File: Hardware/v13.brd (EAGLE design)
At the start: 50 x 50 mm, 90 parts, among them J1 22-27-2081-08, J2 22-27-2031-03

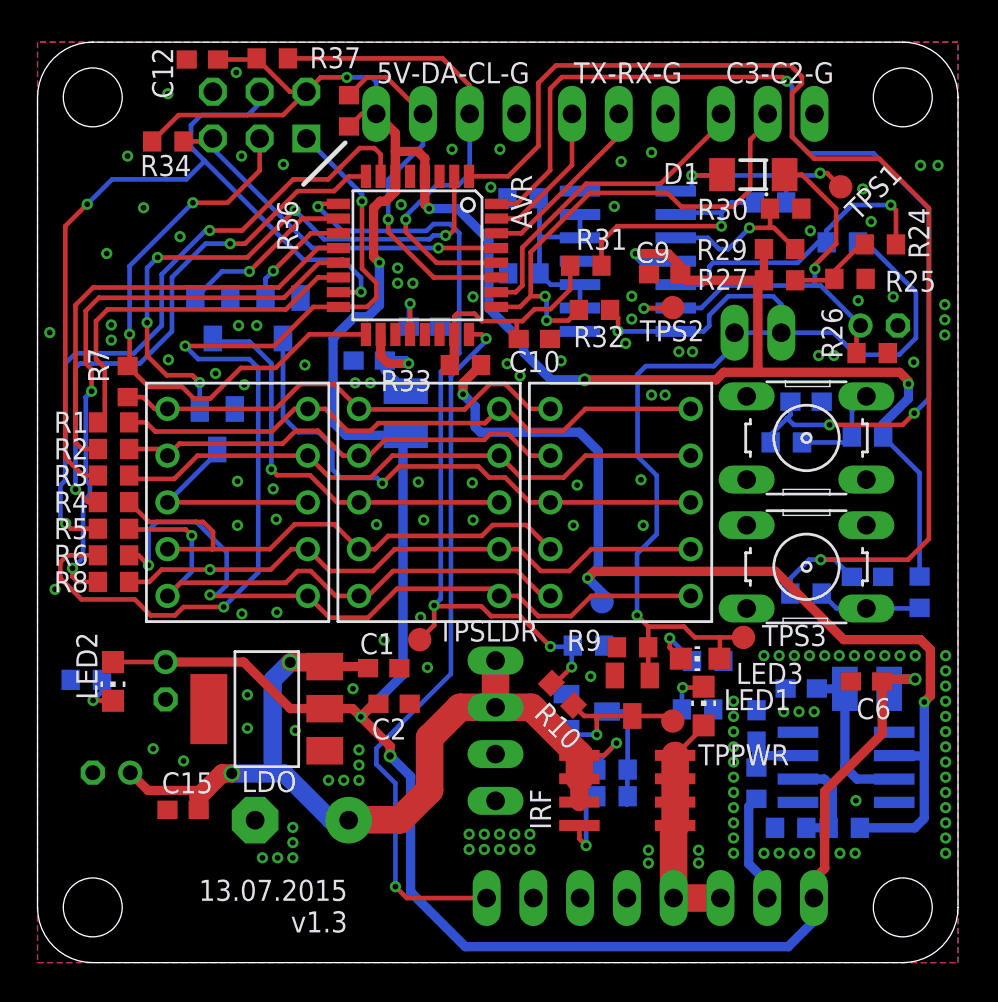
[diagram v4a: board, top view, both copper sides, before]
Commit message: changed the place of some resistors
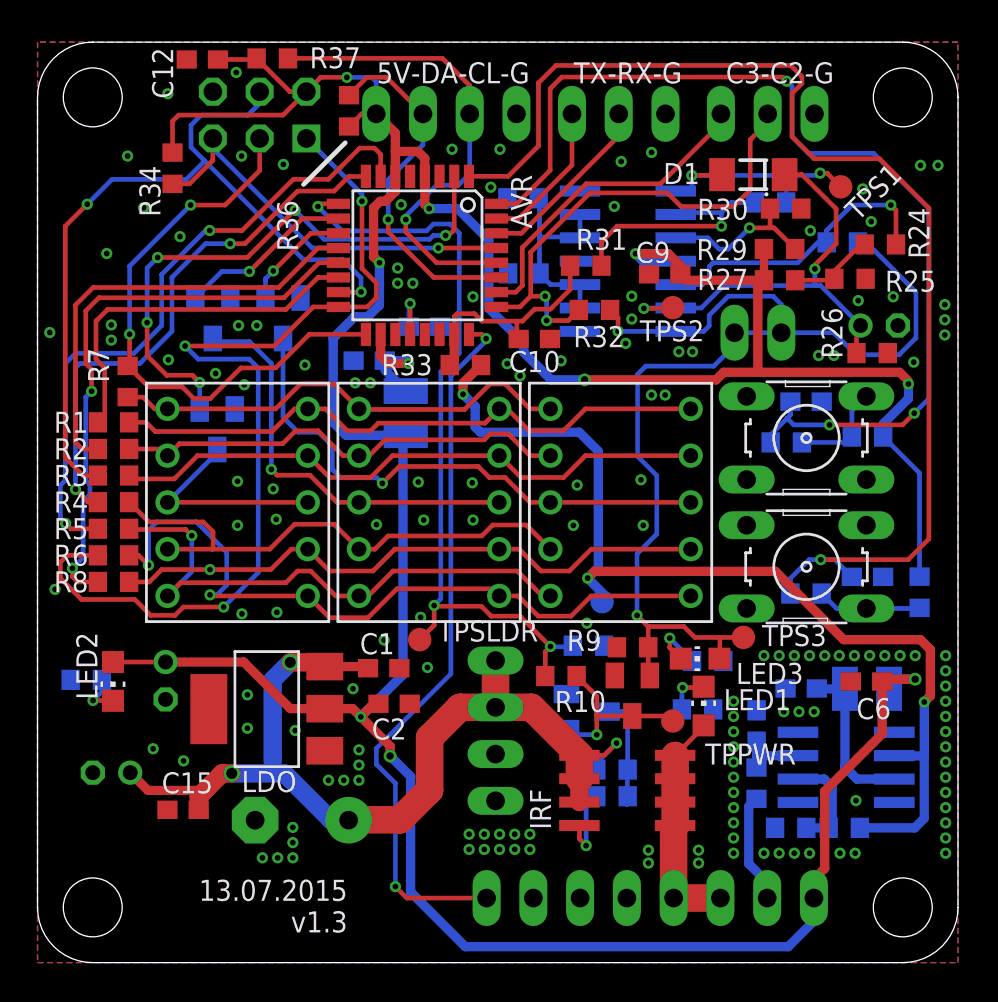
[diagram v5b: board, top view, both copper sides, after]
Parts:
- moved R34 1.48 mm to (7.33, 43.2), turned to 270 degrees
- moved R10 0.99 mm to (28.4, 15.6), turned to 180 degrees
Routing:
- net RST: track 19.9 -> 22.1 mm
- net N$16: track 8.96 -> 10.1 mm
- net LOETKOLBEN: track 43.9 -> 43.0 mm, vias 4 -> 3
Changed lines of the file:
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@@
 <layer number="20" name="Dimension" color="15" fill="1" visible="yes" active="yes"/>
 <layer number="21" name="tPlace" color="7" fill="1" visible="yes" active="yes"/>
-<layer number="22" name="bPlace" color="7" fill="1" visible="no" active="yes"/>
+<layer number="22" name="bPlace" color="7" fill="1" visible="yes" active="yes"/>
 <layer number="23" name="tOrigins" color="15" fill="1" visible="yes" active="yes"/>
-<layer number="24" name="bOrigins" color="15" fill="1" visible="no" active="yes"/>
+<layer number="24" name="bOrigins" color="15" fill="1" visible="yes" active="yes"/>
 <layer number="25" name="tNames" color="7" fill="1" visible="yes" active="yes"/>
 <layer number="26" name="bNames" color="7" fill="1" visible="no" active="yes"/>
@@
 <attribute name="VALUE" x="23.1775" y="31.75" size="1.27" layer="28" rot="MR270"/>
 </element>
-<element name="R34" library="rcl" package="R0603" value="10k" x="7.08025" y="44.605575" smashed="yes">
-<attribute name="NAME" x="5.578475" y="42.7228" size="1.143" layer="25" font="vector" ratio="15"/>
-<attribute name="VALUE" x="6.44525" y="42.700575" size="1.27" layer="27"/>
+<element name="R34" library="rcl" package="R0603" value="10k" x="7.33425" y="43.151425" smashed="yes" rot="R270">
+<attribute name="NAME" x="5.534025" y="43.291125" size="1.143" layer="25" font="vector" ratio="15" rot="R270"/>
+<attribute name="VALUE" x="5.42925" y="43.786425" size="1.27" layer="27" rot="R270"/>
 </element>
 <element name="DIS1" library="display-hp" package="HDSP-E" value="SC39-11SRWA" x="31.67" y="25" smashed="yes">
@@
 </element>
 <element name="R33" library="rcl" package="R0603" value="10k" x="23.241" y="32.458025" smashed="yes" rot="R180">
-<attribute name="NAME" x="18.63725" y="31.0388" size="1.143" layer="25" font="vector" ratio="15"/>
+<attribute name="NAME" x="18.678525" y="31.905575" size="1.143" layer="25" font="vector" ratio="15"/>
 <attribute name="VALUE" x="23.876" y="34.363025" size="1.27" layer="27" rot="R180"/>
 </element>
@@
 <attribute name="VALUE" x="30.56255" y="15.313025" size="1.27" layer="28" rot="MR0"/>
 </element>
-<element name="R10" library="rcl" package="R0603" value="10k" x="28.514675" y="14.576425" smashed="yes" rot="R135">
-<attribute name="NAME" x="29.670371875" y="12.275046875" size="1.143" layer="25" font="vector" ratio="15" rot="R135"/>
-<attribute name="VALUE" x="30.310725" y="15.47445" size="1.27" layer="27" rot="R135"/>
+<element name="R10" library="rcl" package="R0603" value="10k" x="28.432125" y="15.567025" smashed="yes" rot="R180">
+<attribute name="NAME" x="30.87664375" y="14.756903125" size="1.143" layer="25" font="vector" ratio="15" rot="R180"/>
+<attribute name="VALUE" x="29.067121875" y="17.472021875" size="1.27" layer="27" rot="R180"/>
 </element>
 <element name="R15" library="rcl" package="R0603" value="10k" x="31.2039" y="10.48385" smashed="yes" rot="MR0">
@@
 <element name="TPPWR" library="testpad" package="B1,27" value="TPB1,27" x="34.5059" y="13.12545" smashed="yes">
 <attribute name="TP_SIGNAL_NAME" value="" x="33.8709" y="11.22045" size="1" layer="37"/>
-<attribute name="NAME" x="35.893375" y="10.715625" size="1.143" layer="25" font="vector" ratio="15"/>
+<attribute name="NAME" x="36.26485" y="10.7569" size="1.143" layer="25" font="vector" ratio="15"/>
 <attribute name="VALUE" x="33.8709" y="12.36345" size="0.0254" layer="27"/>
 </element>
@@
 <wire x1="18.272125" y1="14.062075" x2="18.5175" y2="14.062075" width="0.508" layer="1"/>
 <wire x1="13.335" y1="46.0375" x2="7.662175" y2="46.0375" width="0.254" layer="1"/>
-<wire x1="7.662175" y1="46.0375" x2="6.23025" y2="44.605575" width="0.254" layer="1"/>
 <wire x1="9.8035" y1="49.056925" x2="11.84365" y2="49.056925" width="0.254" layer="1"/>
 <wire x1="11.84365" y1="49.056925" x2="11.903975" y2="49.11725" width="0.254" layer="1"/>
 <wire x1="14.605" y1="47.3075" x2="13.713725" y2="47.3075" width="0.254" layer="1"/>
 <wire x1="13.713725" y1="47.3075" x2="11.903975" y2="49.11725" width="0.254" layer="1"/>
+<wire x1="7.662175" y1="46.0375" x2="7.33425" y2="45.709575" width="0.254" layer="1"/>
+<wire x1="7.33425" y1="45.709575" x2="7.33425" y2="44.001425" width="0.254" layer="1"/>
 </signal>
 <signal name="GND">
@@
 <via x="44.45635" y="8.8011" extent="1-16" drill="0.31"/>
 <contactref element="C6" pad="1"/>
-<via x="30.0482" y="15.547975" extent="1-16" drill="0.31"/>
+<via x="29.841825" y="18.437225" extent="1-16" drill="0.31"/>
 <via x="37.8079" y="14.1986" extent="1-16" drill="0.31"/>
 <via x="39.4589" y="16.6751" extent="1-16" drill="0.31"/>
@@
 <contactref element="R10" pad="2"/>
 <wire x1="21.9075" y1="19.7612" x2="21.9075" y2="32.09925" width="0.254" layer="16"/>
-<via x="29.016325" y="16.055975" extent="1-16" drill="0.31"/>
-<wire x1="29.016325" y1="16.055975" x2="29.016325" y2="17.1568" width="0.254" layer="16"/>
 <wire x1="29.016325" y1="17.1568" x2="29.07755" y2="17.218025" width="0.254" layer="16"/>
 <wire x1="29.016325" y1="17.1568" x2="27.874225" y2="17.1568" width="0.254" layer="16"/>
@@
 <via x="21.54555" y="19.39925" extent="1-16" drill="0.31"/>
 <wire x1="21.54555" y1="19.39925" x2="21.9075" y2="19.7612" width="0.254" layer="16"/>
-<wire x1="29.016325" y1="16.055975" x2="28.137815625" y2="15.177465625" width="0.254" layer="1"/>
-<wire x1="28.137815625" y1="15.177465625" x2="27.91363125" y2="15.177465625" width="0.254" layer="1"/>
 <contactref element="TPSLDR" pad="TP"/>
 <wire x1="20.761325" y1="17.541875" x2="21.54555" y2="18.3261" width="0.254" layer="1"/>
@@
 <wire x1="22.907625" y1="39.624" x2="22.412325" y2="40.1193" width="0.254" layer="16"/>
 <wire x1="22.412325" y1="40.1193" x2="21.504275" y2="40.1193" width="0.254" layer="16"/>
+<wire x1="27.582125" y1="15.567025" x2="27.582125" y2="16.8919" width="0.254" layer="1"/>
+<wire x1="27.582125" y1="16.8919" x2="27.860625" y2="17.1704" width="0.254" layer="1"/>
 </signal>
 <signal name="MOSI">
@@
 <contactref element="R7" pad="2"/>
 <wire x1="17.8375" y1="34.1249" x2="17.820725" y2="34.108125" width="0.254" layer="1"/>
-<via x="8.43915" y="41.275" extent="1-16" drill="0.31"/>
+<via x="8.315325" y="41.151175" extent="1-16" drill="0.31"/>
 <wire x1="8.493125" y1="30.63875" x2="7.858125" y2="31.27375" width="0.254" layer="1"/>
 <wire x1="8.493125" y1="30.63875" x2="9.37895" y2="30.63875" width="0.254" layer="1"/>
@@
 <wire x1="12.938125" y1="32.305625" x2="14.7574" y2="34.1249" width="0.254" layer="1"/>
 <wire x1="5.000625" y1="34.13125" x2="5.000625" y2="37.836475" width="0.254" layer="16"/>
-<wire x1="5.000625" y1="37.836475" x2="8.43915" y2="41.275" width="0.254" layer="16"/>
-<wire x1="12.065" y1="43.02125" x2="10.31875" y2="41.275" width="0.254" layer="1"/>
-<wire x1="10.31875" y1="41.275" x2="8.43915" y2="41.275" width="0.254" layer="1"/>
+<wire x1="5.000625" y1="37.836475" x2="8.315325" y2="41.151175" width="0.254" layer="16"/>
+<wire x1="12.065" y1="43.02125" x2="10.194925" y2="41.151175" width="0.254" layer="1"/>
+<wire x1="10.194925" y1="41.151175" x2="8.315325" y2="41.151175" width="0.254" layer="1"/>
 <wire x1="12.065" y1="43.02125" x2="12.065" y2="44.7675" width="0.254" layer="1"/>
 <via x="5.000625" y="34.13125" extent="1-16" drill="0.31"/>
@@
 <wire x1="14.92255" y1="38.8175" x2="21.7742" y2="38.8175" width="0.254" layer="16"/>
 <via x="21.7742" y="38.8175" extent="1-16" drill="0.31"/>
-<wire x1="7.93025" y1="44.605575" x2="9.363075" y2="44.605575" width="0.254" layer="1"/>
-<wire x1="9.363075" y1="44.605575" x2="9.525" y2="44.7675" width="0.254" layer="1"/>
+<wire x1="7.33425" y1="42.301425" x2="8.24955" y2="42.301425" width="0.254" layer="1"/>
+<wire x1="8.24955" y1="42.301425" x2="9.525" y2="43.576875" width="0.254" layer="1"/>
+<wire x1="9.525" y1="43.576875" x2="9.525" y2="44.7675" width="0.254" layer="1"/>
 </signal>
 <signal name="12V">
@@
 <contactref element="PWR-Q2" pad="3"/>
 <wire x1="28.29945" y1="12.686625" x2="28.7323" y2="12.686625" width="0.254" layer="16"/>
-<wire x1="29.115715625" y1="13.97538125" x2="29.694046875" y2="13.39705" width="0.254" layer="1"/>
-<wire x1="29.694046875" y1="13.39705" x2="30.3784" y2="13.39705" width="0.254" layer="1"/>
 <wire x1="30.3784" y1="13.39705" x2="32.3088" y2="13.39705" width="0.254" layer="1"/>
 <wire x1="28.7323" y1="12.686625" x2="29.036425" y2="12.3825" width="0.254" layer="16"/>
@@
 <wire x1="34.5059" y1="13.12545" x2="34.2343" y2="13.39705" width="0.254" layer="1"/>
 <wire x1="34.2343" y1="13.39705" x2="32.3088" y2="13.39705" width="0.254" layer="1"/>
+<wire x1="30.3784" y1="13.39705" x2="30.3784" y2="14.47075" width="0.254" layer="1"/>
+<wire x1="30.3784" y1="14.47075" x2="29.282125" y2="15.567025" width="0.254" layer="1"/>
 </signal>
 <signal name="N$22">

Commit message: change some resistor values moved the leds to lower left corner
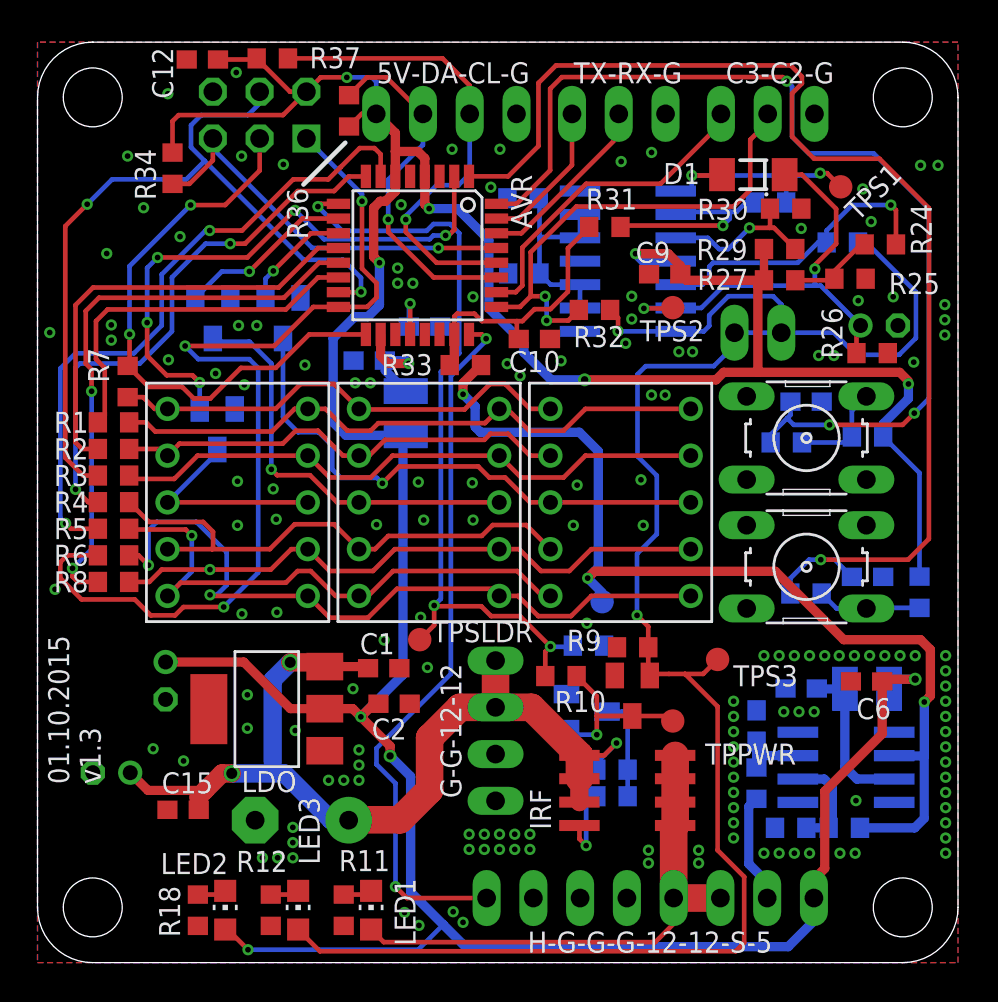
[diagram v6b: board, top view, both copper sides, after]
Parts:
- R31: value 20k -> 10k
- R36, R37: value 4k7 -> 10k
- moved R12 27.3 mm to (12.7, 2.85), flipped to the top, turned to 270 degrees
- moved LED3 25.8 mm to (14.2, 2.85), turned to 0 degrees
- moved R11 22.1 mm to (16.6, 2.85), flipped to the top, turned to 90 degrees
- moved LED1 21.2 mm to (18.1, 2.85)
- moved R18 13.9 mm to (8.71, 2.85), flipped to the top, turned to 90 degrees
- moved LED2 13.8 mm to (10.2, 2.85), turned to 0 degrees
- moved R31 2.34 mm to (30.8, 40.0)
- moved TPS3 1.84 mm to (36.9, 16.5)
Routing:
- net SAFETY: track 61.3 -> 99.6 mm
- net PWM_OUT: track 12.7 -> 28.9 mm
- net VCC: track 199.0 -> 209.0 mm, vias 9 -> 10
- net THERMO0: track 12.3 -> 14.8 mm
- net N$3: track 13.5 -> 11.1 mm
- net N$2: track 3.10 -> 1.57 mm, vias 1 -> 0
- net P-FET_GATE: track 6.86 -> 5.56 mm
- net N$24: track 2.41 -> 1.57 mm, vias 1 -> 0
- net N$25: track 2.36 -> 1.57 mm, vias 1 -> 0
- net PC2: track 27.5 -> 26.9 mm
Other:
- board text added: "01.10.2015 v1.3"
- board text added: "G-G-12-12"
- board text added: "H-G-G-G-12-12-S-5"
- board text removed: "13.07.2015 v1.3"

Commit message: added unmounted resistors around hall sensor wire added more labels changed some wires to comply with elecrow drc added heat sink for low drop, which is not connected to anything else
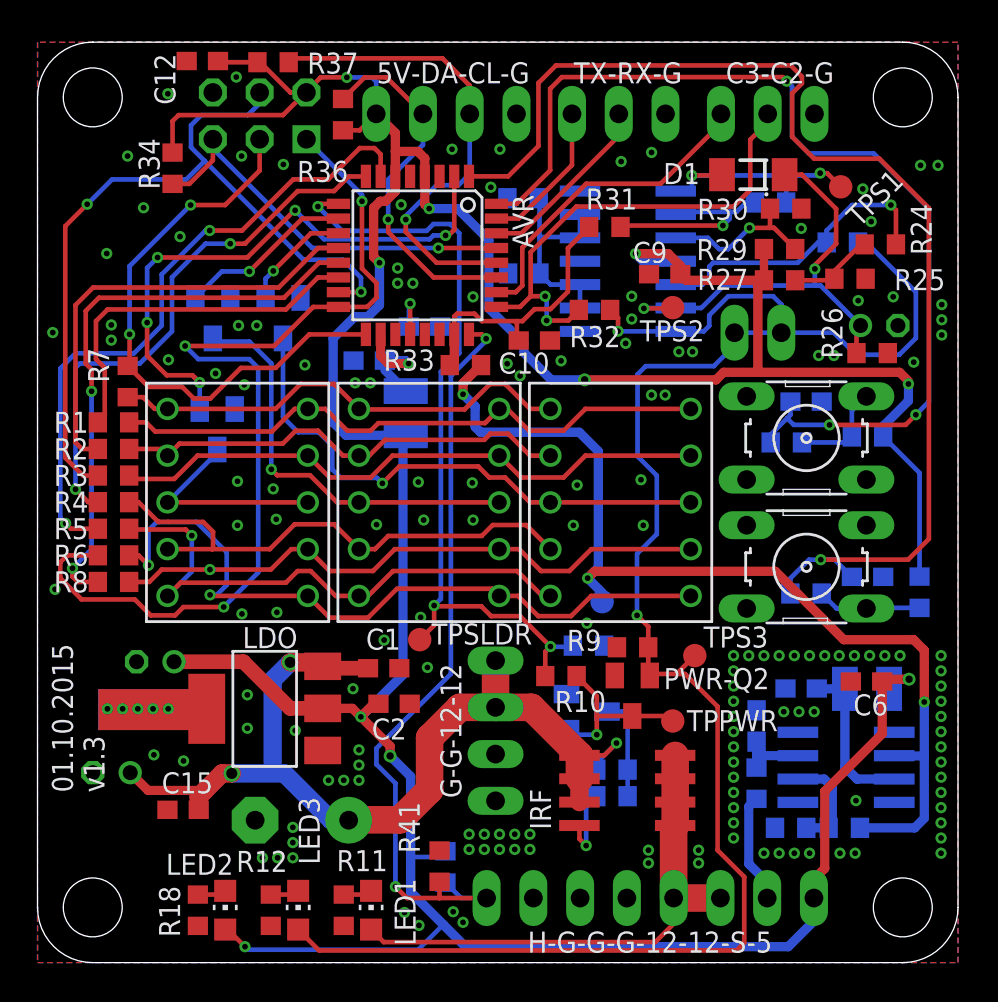
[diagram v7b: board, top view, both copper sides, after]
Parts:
- added R38: n.m., rcl:R0603
- added R41: n.m, rcl:R0603
- moved TPS3 1.26 mm to (35.7, 16.7)
- moved C13 1.17 mm to (6.40, 16.3), turned to 0 degrees
- moved R36 0.39 mm to (16.6, 46.1)
- moved R37 0.21 mm to (12.8, 48.9)
- moved LDO 0.12 mm to (12.3, 13.8)
- moved C10 0.08 mm to (27.0, 33.8)
- moved C12 0.08 mm to (8.95, 49.0)
- renumbered DISP-Q1 to Q1, DISP-Q2 to Q2, DISP-Q3 to Q3
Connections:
- net GND: now also R41.1
- net HALL: now also R38.1, R41.2
- net VCC: now also R38.2
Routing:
- net HALL: track 38.9 -> 42.4 mm
- net VCC: track 209.0 -> 209.9 mm
- net SAFETY: track 99.6 -> 98.9 mm
